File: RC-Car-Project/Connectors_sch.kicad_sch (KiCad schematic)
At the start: 14 parts, among them J1 Conn_01x02_Pin, J10 ANT_IF, J11 Conn_01x02, J12 Conn_01x02, J2 Conn_01x02_Pin, J3 Conn_01x02_Pin, J4 Conn_01x02_Pin, J5 MCU_IF, J6 Conn_01x02, J7 Conn_01x02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

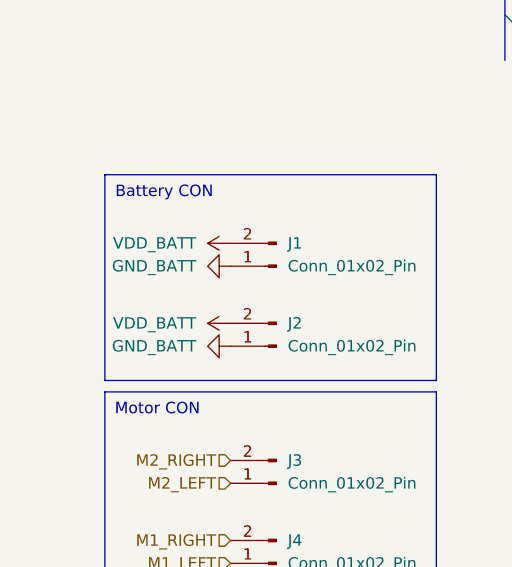
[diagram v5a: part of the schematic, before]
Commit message: Fix Bat connections to sw
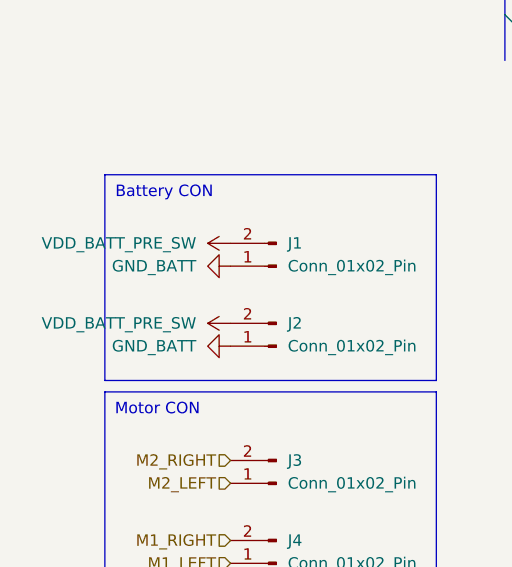
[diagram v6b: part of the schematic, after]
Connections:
- net VDD_BATT is gone; now on net VDD_BATT_PRE_SW: J1.2 (Pin_2), J2.2 (Pin_2)
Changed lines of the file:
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@@
+	(symbol
+		(lib_id "power:+3V3")
+		(at 73.66 92.71 90)
+		(unit 1)
+		(exclude_from_sim no)
+		(in_bom yes)
+		(on_board yes)
+		(dnp no)
+		(fields_autoplaced yes)
+		(property "Reference" "#PWR011"
+			(at 77.47 92.71 0)
+			(effects
+				(font
+					(size 1.27 1.27)
+				)
+				(hide yes)
+			)
+		)
+		(property "Value" "VDD_BATT_PRE_SW"
+			(at 69.85 92.7099 90)
+			(effects
+				(font
+					(size 1.27 1.27)
+				)
+				(justify left)
+			)
+		)
+		(property "Footprint" ""
+			(at 73.66 92.71 0)
+			(effects
+				(font
+					(size 1.27 1.27)
+				)
+				(hide yes)
+			)
+		)
+		(property "Datasheet" ""
+			(at 73.66 92.71 0)
+			(effects
+				(font
+					(size 1.27 1.27)
+				)
+				(hide yes)
+			)
+		)
+		(property "Description" "Power symbol creates a global label with name \"+3V3\""
+			(at 73.66 92.71 0)
+			(effects
+				(font
+					(size 1.27 1.27)
+				)
+				(hide yes)
+			)
+		)
+		(pin "1"
+		)
+		(instances
+			(project "RC-Car-Project"
+				(path "/ba870fd1-751d-4755-8e1a-1ea86ca9e2f6/47812da9-b622-4bda-8507-4e09448e1ff5"
+					(reference "#PWR011")
+					(unit 1)
+				)
+			)
+		)
+	)
 	(symbol
 		(lib_id "power:+3V3")
@@
 	)
 	(symbol
-		(lib_id "power:+3V3")
-		(at 73.66 92.71 90)
-		(unit 1)
-		(exclude_from_sim no)
-		(in_bom yes)
-		(on_board yes)
-		(dnp no)
-		(fields_autoplaced yes)
-		(property "Reference" "#PWR011"
-			(at 77.47 92.71 0)
-			(effects
-				(font
-					(size 1.27 1.27)
-				)
-				(hide yes)
-			)
-		)
-		(property "Value" "VDD_BATT"
-			(at 69.85 92.7099 90)
+		(lib_id "Connector_Generic:Conn_01x02")
+		(at 154.94 107.95 0)
+		(unit 1)
+		(exclude_from_sim no)
+		(in_bom yes)
+		(on_board yes)
+		(dnp no)
+		(fields_autoplaced yes)
+		(property "Reference" "J12"
+			(at 157.48 107.9499 0)
 			(effects
 				(font
@@
 			)
 		)
+		(property "Value" "Conn_01x02"
+			(at 157.48 110.4899 0)
+			(effects
+				(font
+					(size 1.27 1.27)
+				)
+				(justify left)
+			)
+		)
+		(property "Footprint" "Connector_JST:JST_XH_B2B-XH-AM_1x02_P2.50mm_Vertical"
+			(at 154.94 107.95 0)
+			(effects
+				(font
+					(size 1.27 1.27)
+				)
+				(hide yes)
+			)
+		)
+		(property "Datasheet" "~"
+			(at 154.94 107.95 0)
+			(effects
+				(font
+					(size 1.27 1.27)
+				)
+				(hide yes)
+			)
+		)
+		(property "Description" "Generic connector, single row, 01x02, script generated (kicad-library-utils/schlib/autogen/connector/)"
+			(at 154.94 107.95 0)
+			(effects
+				(font
+					(size 1.27 1.27)
+				)
+				(hide yes)
+			)
+		)
+		(pin "1"
+		)
+		(pin "2"
+		)
+		(instances
+			(project "RC-Car-Project"
+				(path "/ba870fd1-751d-4755-8e1a-1ea86ca9e2f6/47812da9-b622-4bda-8507-4e09448e1ff5"
+					(reference "J12")
+					(unit 1)
+				)
+			)
+		)
+	)
+	(symbol
+		(lib_id "power:GND")
+		(at 73.66 95.25 270)
+		(unit 1)
+		(exclude_from_sim no)
+		(in_bom yes)
+		(on_board yes)
+		(dnp no)
+		(fields_autoplaced yes)
+		(property "Reference" "#PWR012"
+			(at 67.31 95.25 0)
+			(effects
+				(font
+					(size 1.27 1.27)
+				)
+				(hide yes)
+			)
+		)
+		(property "Value" "GND_BATT"
+			(at 69.85 95.2499 90)
+			(effects
+				(font
+					(size 1.27 1.27)
+				)
+				(justify right)
+			)
+		)
 		(property "Footprint" ""
-			(at 73.66 92.71 0)
+			(at 73.66 95.25 0)
 			(effects
 				(font
@@
 		)
 		(property "Datasheet" ""
-			(at 73.66 92.71 0)
-			(effects
-				(font
-					(size 1.27 1.27)
-				)
-				(hide yes)
-			)
-		)
-		(property "Description" "Power symbol creates a global label with name \"+3V3\""
-			(at 73.66 92.71 0)
+			(at 73.66 95.25 0)
+			(effects
+				(font
+					(size 1.27 1.27)
+				)
+				(hide yes)
+			)
+		)
+		(property "Description" "Power symbol creates a global label with name \"GND\" , ground"
+			(at 73.66 95.25 0)
 			(effects
 				(font
@@
 			(project "RC-Car-Project"
 				(path "/ba870fd1-751d-4755-8e1a-1ea86ca9e2f6/47812da9-b622-4bda-8507-4e09448e1ff5"
-					(reference "#PWR011")
+					(reference "#PWR012")
 					(unit 1)
 				)
@@
 			)
 		)
-		(property "Value" "VDD_BATT"
+		(property "Value" "VDD_BATT_PRE_SW"
 			(at 69.85 101.5999 90)
 			(effects
@@
 					(unit 1)
 				)
-			)
-		)
-	)
-	(symbol
-		(lib_id "Connector_Generic:Conn_01x02")
-		(at 154.94 107.95 0)
-		(unit 1)
-		(exclude_from_sim no)
-		(in_bom yes)
-		(on_board yes)
-		(dnp no)
-		(fields_autoplaced yes)
-		(property "Reference" "J12"
-			(at 157.48 107.9499 0)
-			(effects
-				(font
-					(size 1.27 1.27)
-				)
-				(justify left)
-			)
-		)
-		(property "Value" "Conn_01x02"
-			(at 157.48 110.4899 0)
-			(effects
-				(font
-					(size 1.27 1.27)
-				)
-				(justify left)
-			)
-		)
-		(property "Footprint" "Connector_JST:JST_XH_B2B-XH-AM_1x02_P2.50mm_Vertical"
-			(at 154.94 107.95 0)
-			(effects
-				(font
-					(size 1.27 1.27)
-				)
-				(hide yes)
-			)
-		)
-		(property "Datasheet" "~"
-			(at 154.94 107.95 0)
-			(effects
-				(font
-					(size 1.27 1.27)
-				)
-				(hide yes)
-			)
-		)
-		(property "Description" "Generic connector, single row, 01x02, script generated (kicad-library-utils/schlib/autogen/connector/)"
-			(at 154.94 107.95 0)
-			(effects
-				(font
-					(size 1.27 1.27)
-				)
-				(hide yes)
-			)
-		)
-		(pin "1"
-		)
-		(pin "2"
-		)
-		(instances
-			(project "RC-Car-Project"
-				(path "/ba870fd1-751d-4755-8e1a-1ea86ca9e2f6/47812da9-b622-4bda-8507-4e09448e1ff5"
-					(reference "J12")
-					(unit 1)
-				)
-			)
-		)
-	)
-	(symbol
-		(lib_id "power:GND")
-		(at 73.66 95.25 270)
-		(unit 1)
-		(exclude_from_sim no)
-		(in_bom yes)
-		(on_board yes)
-		(dnp no)
-		(fields_autoplaced yes)
-		(property "Reference" "#PWR012"
-			(at 67.31 95.25 0)
-			(effects
-				(font
-					(size 1.27 1.27)
-				)
-				(hide yes)
-			)
-		)
-		(property "Value" "GND_BATT"
-			(at 69.85 95.2499 90)
-			(effects
-				(font
-					(size 1.27 1.27)
-				)
-				(justify right)
-			)
-		)
-		(property "Footprint" ""
-			(at 73.66 95.25 0)
-			(effects
-				(font
-					(size 1.27 1.27)
-				)
-				(hide yes)
-			)
-		)
-		(property "Datasheet" ""
-			(at 73.66 95.25 0)
-			(effects
-				(font
-					(size 1.27 1.27)
-				)
-				(hide yes)
-			)
-		)
-		(property "Description" "Power symbol creates a global label with name \"GND\" , ground"
-			(at 73.66 95.25 0)
-			(effects
-				(font
-					(size 1.27 1.27)
-				)
-				(hide yes)
-			)
-		)
-		(pin "1"
-		)
-		(instances
-			(project "RC-Car-Project"
-				(path "/ba870fd1-751d-4755-8e1a-1ea86ca9e2f6/47812da9-b622-4bda-8507-4e09448e1ff5"
-					(reference "#PWR012")
-					(unit 1)
-				)

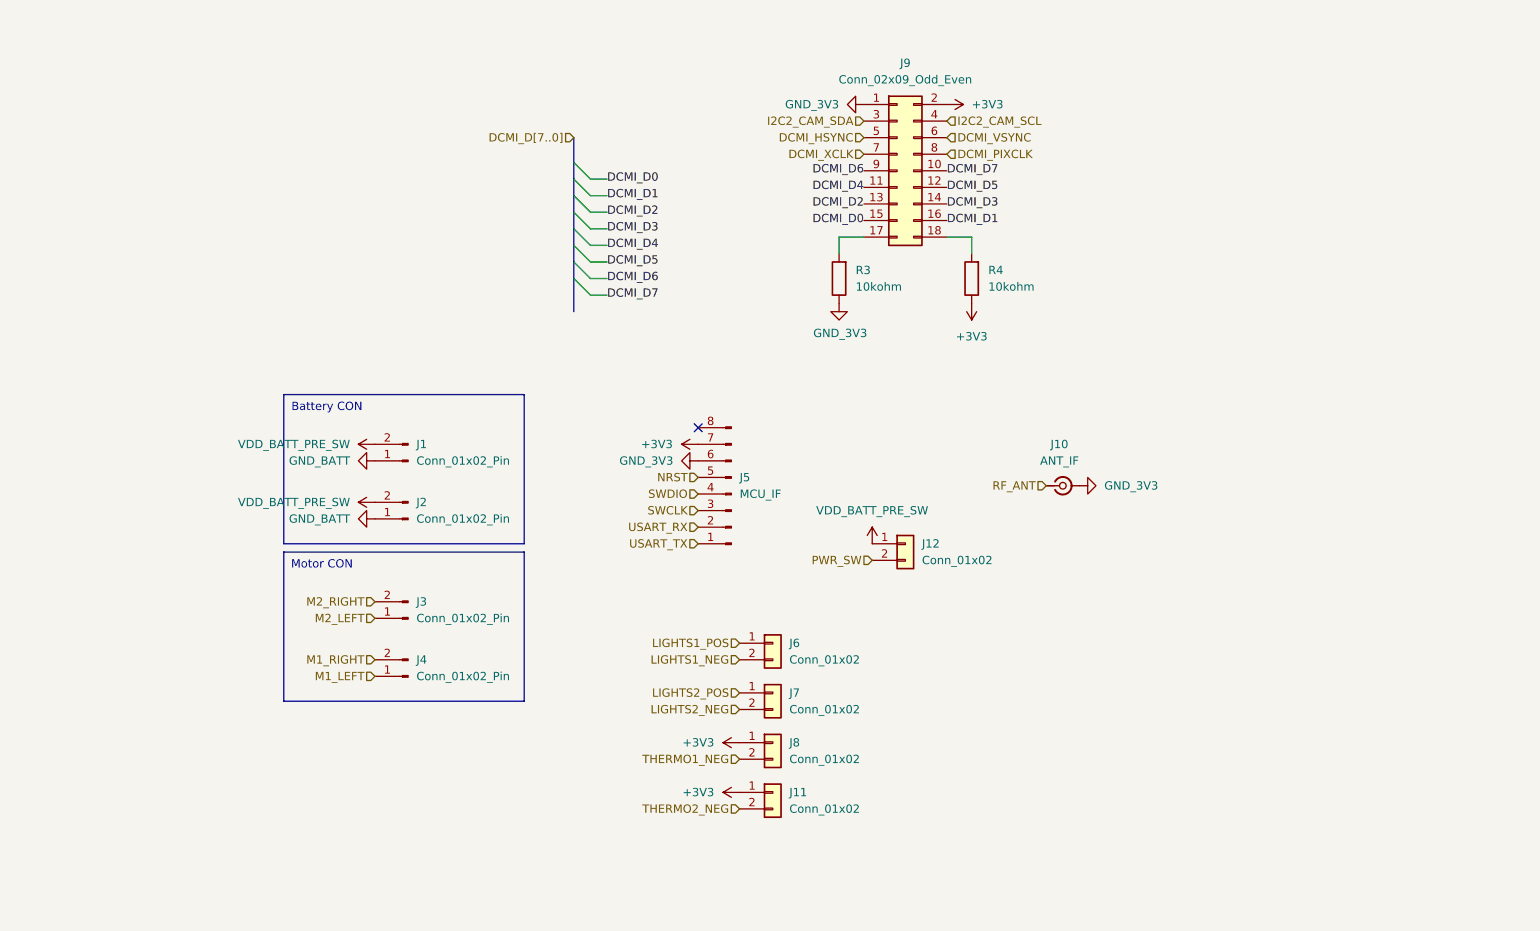
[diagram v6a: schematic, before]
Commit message: Added functionality to the STM32 on the tank PCB
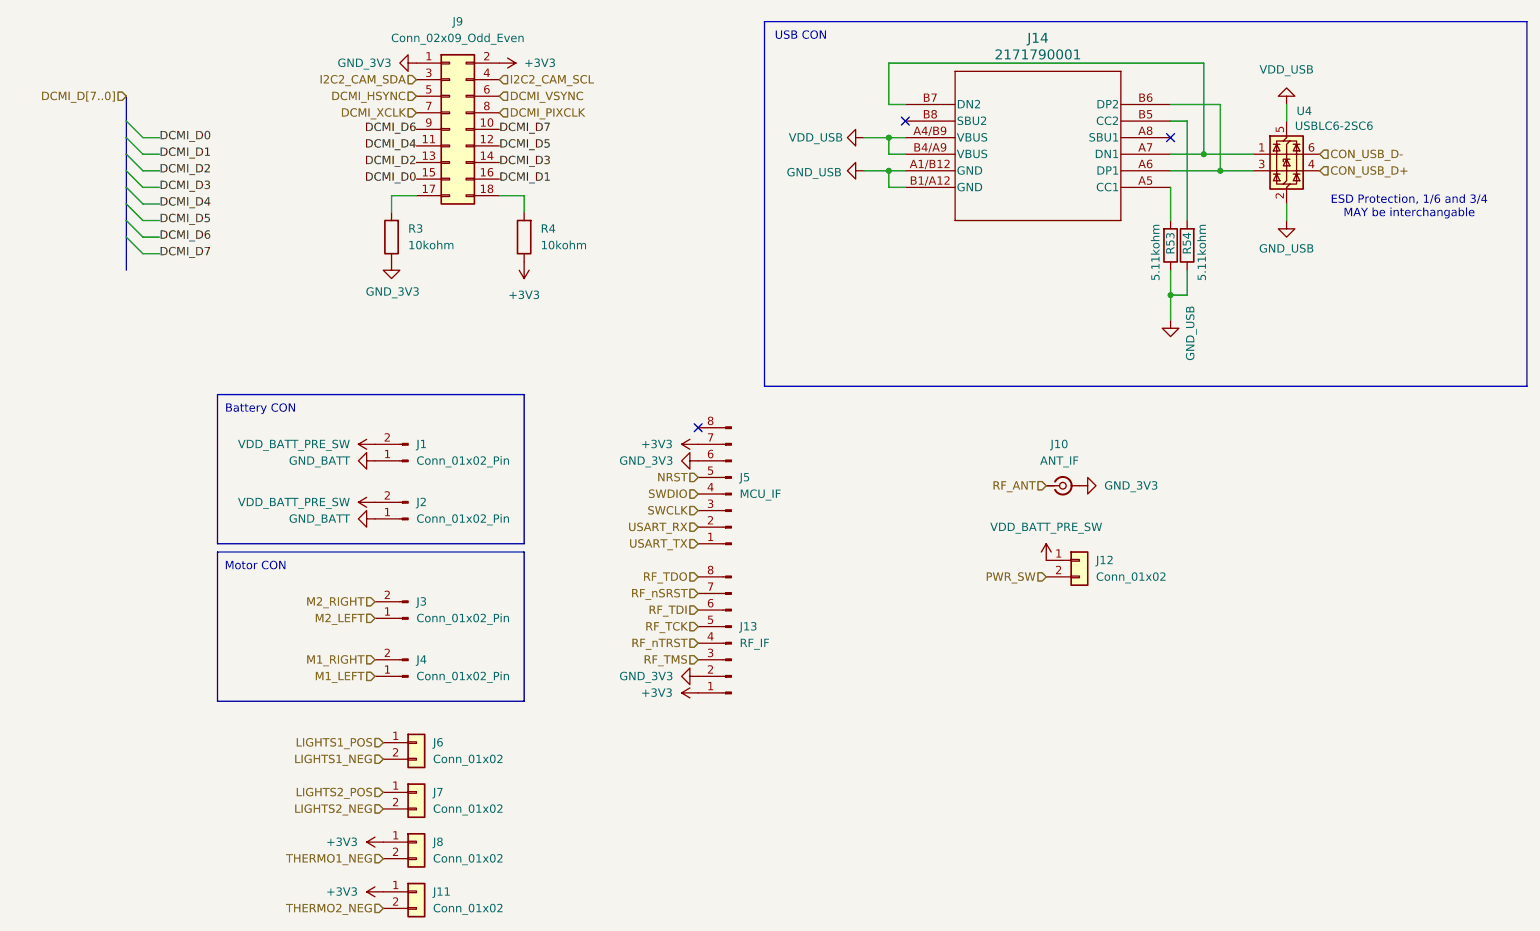
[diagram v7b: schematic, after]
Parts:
- added J13: RF_IF, Connector_PinHeader_2.54mm:PinHeader_2x04_P2.54mm_Vertical, symbol Connector:Conn_01x08_Pin
- added J14: 2171790001, USB-C 2171790001:2171790001_MOL, symbol USB-C 2171790001:2171790001
- added R53, R54: 5.11kohm, Resistor_SMD:R_0603_1608Metric, symbol Device:R
- added U4: USBLC6-2SC6, Package_TO_SOT_SMD:SOT-23-6, symbol Power_Protection:USBLC6-2SC6
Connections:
- net +3V3: now also J13.1 (Pin_1)
- net GND_3V3: now also J13.2 (Pin_2)
- new net: J14.A5 (CC1), R53.2
- new net: J14.A6 (DP1), J14.B6 (DP2), U4.3 (I/O2)
- new net: J14.A7 (DN1), J14.B7 (DN2), U4.1 (I/O1)
- new net: J14.B5 (CC2), R54.2
- new net CON_USB_D+: U4.4 (I/O2)
- new net CON_USB_D-: U4.6 (I/O1)
- new net GND_USB: J14.A1/B12 (GND), J14.B1/A12 (GND), R53.1, R54.1, U4.2 (GND)
- new net RF_TCK: J13.5 (Pin_5)
- new net RF_TDI: J13.6 (Pin_6)
- new net RF_TDO: J13.8 (Pin_8)
- new net RF_TMS: J13.3 (Pin_3)
- new net RF_nSRST: J13.7 (Pin_7)
- new net RF_nTRST: J13.4 (Pin_4)
- new net VDD_USB: J14.A4/B9 (VBUS), J14.B4/A9 (VBUS), U4.5 (VBUS)
- no-connect marks 1 -> 3
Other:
- note added: "ESD Protection, 1/6 and 3/4 MAY be interchangable"
- note added: "USB CON"
- moved on the sheet: J11, J12, J6, J7, J8, J9, R3, R4

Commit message: I'm tired boss
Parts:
- removed J14: 2171790001, USB-C 2171790001:2171790001_MOL, symbol USB-C 2171790001:2171790001
- added J15: USB4120-03-C_REVA, USB4120-03-C:GCT_USB4120-03-C_REVA, symbol USB4120-03-C:USB4120-03-C_REVA
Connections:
- net GND_USB: now also J15.A1 (GND_A), J15.A12 (GND_A__1), J15.B1 (GND_B), J15.B12 (GND_B__1)
- net VDD_USB: now also J15.A4 (VBUS_A), J15.A9 (VBUS_A__1), J15.B4 (VBUS_B), J15.B9 (VBUS_B__1)
- net at R53.2: now also J15.B5 (CC2)
- net at U4.3 (I/O2): now also J15.A6 (D1+), J15.B6 (D2+)
- net at U4.1 (I/O1): now also J15.A7 (D1-), J15.B7 (D2-)
- net at R54.2: now also J15.A5 (CC1)
- no-connect marks 3 -> 7
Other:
- moved on the sheet: R53, R54, U4
